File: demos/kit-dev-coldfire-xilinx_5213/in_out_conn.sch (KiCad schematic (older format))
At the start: 73 parts, among them J1 JACK_2P, SW1 SW_PUSH, SW2 SW_PUSH, U3 MAX202, U4 74HC125, U5 MAX202, U7 PCA82C251, U8 MAX202

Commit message: 3d viewer: minor code cleaning (remove useless #include ) dialog_track_via_size: set minimal size  and make dialog resizable. Update demo file.
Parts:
- C22, C23, C24, C25, C26, C27, C28, C30, C31, C32, C33, C34, C35, C36, C41, C43, C44, C45, C46, R23, R28, R30, R31, R32, R33, R34, R35, R36, R38, R47, R48, R49, R50, R53, RCAN1, RCAN2: footprint (none) -> lib_smd:SM0805
- C38, C40: footprint (none) -> discret:C2V8
- CAN_EN1: footprint (none) -> pin_array:PIN_ARRAY_2X2
- CAN_TERM1, LED_EN1, VX_EN1: footprint (none) -> pin_array:PIN_ARRAY_2X1
- COM_SEL1, COM_SEL2, COM_SEL3: footprint (none) -> pin_array:PIN_ARRAY_3X1
- D7: footprint (none) -> discret:D5
- F1: footprint (none) -> lib_smd:FSUPCMS
- J1: footprint (none) -> connect:JACK_ALIM
- LED1, LED2, LED3, LED4, LED5: footprint (none) -> lib_smd:SM1206POL
- MCU_PORT1: footprint (none) -> pin_array:PIN_ARRAY_30X2
- PULUPEN1, UART_EN0, UART_EN1, UART_EN2: footprint (none) -> pin_array:pin_array_4x2
- RS1, VREF1: footprint (none) -> connect:PINTST
- SW1, SW2: footprint (none) -> discret:SW_PUSH_SMALL
- SW_ONOFF1: footprint (none) -> discret:SW_SPDT
- TB1: footprint (none) -> connect:bornier2
- U3, U5, U8: footprint (none) -> lib_smd:SO16E
- U4: footprint (none) -> lib_smd:SO14E
- U7: footprint (none) -> lib_smd:SO8E
- UARTCAN0, UARTCAN1, UARTCAN2: footprint (none) -> connect:DB9FC
- VR1: footprint (none) -> lib_smd:DPAK5

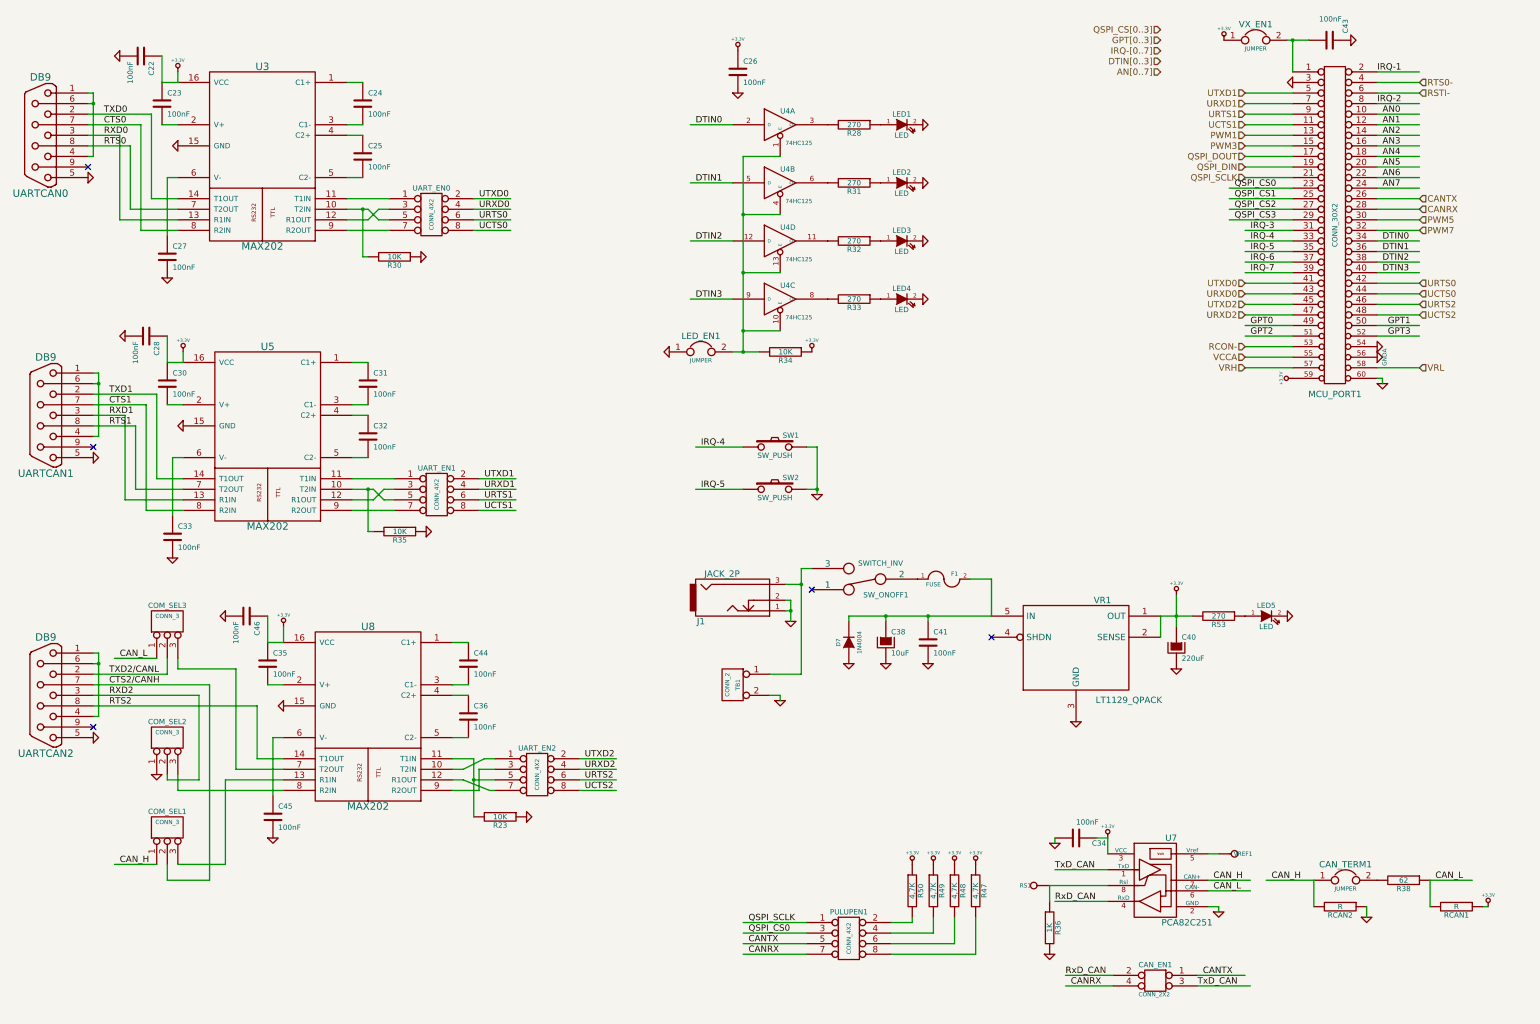
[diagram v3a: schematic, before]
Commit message: demos/ schematic tidying
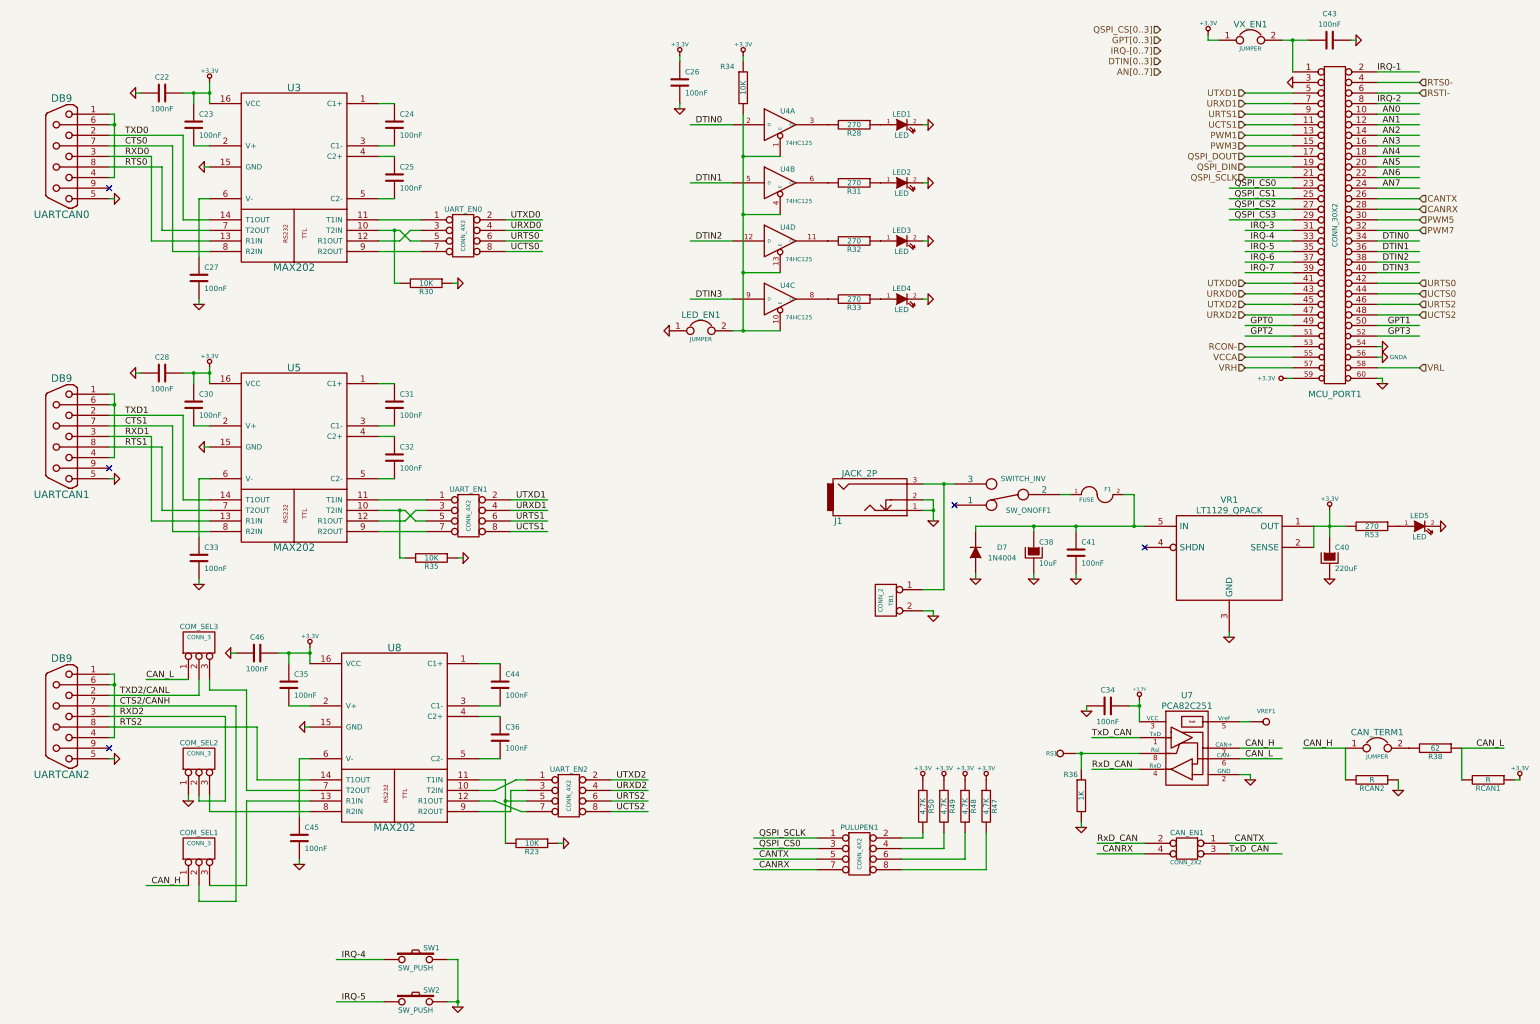
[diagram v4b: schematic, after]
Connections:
- wire segments 259 -> 292
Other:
- moved on the sheet: C22, C23, C24, C25, C26, C27, C28, C30, C31, C32, C33, C34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
